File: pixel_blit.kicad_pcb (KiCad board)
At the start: 4 copper layers, 197.5 x 122 mm, 224 parts, among them CN1 PJ-3059-B, J1 DBT50G-9.5-2P, J10 DB301V-3.5-3P-GN, J11 DB301V-3.5-3P-GN, J12 DB301V-3.5-3P-GN, J13 DB301V-3.5-3P-GN, J14 DB301V-3.5-3P-GN, J15 DB301V-3.5-3P-GN, J16 DB301V-3.5-3P-GN, J17 DB301V-3.5-3P-GN, J18 DB301V-3.5-3P-GN, J19 DB301V-3.5-3P-GN, J2 DBT50G-9.5-2P, J20 DB301V-3.5-3P-GN, J21 DB301V-3.5-3P-GN, J22 DB301V-3.5-3P-GN, J23 DB301V-3.5-3P-GN, J24 DB301V-3.5-3P-GN, J25 DB301V-3.5-3P-GN, J26 DB301V-3.5-3P-GN, J27 DB301V-3.5-3P-GN, J28 DB301V-3.5-3P-GN, J29 DB301V-3.5-3P-GN, J3 DBT50G-9.5-2P, J30 DB301V-3.5-3P-GN, J31 DB301V-3.5-3P-GN, J32 DB301V-3.5-3P-GN, J33 DB301V-3.5-3P-GN, J34 DB301V-3.5-3P-GN, J35 DB301V-3.5-3P-GN, J36 DB301V-3.5-3P-GN, J37 Conn_01x03_Pin, J38 2.54-1*4, J4 DBT50G-9.5-2P, J5 DB301V-3.5-3P-GN, J6 DB301V-3.5-3P-GN, J7 DB301V-3.5-3P-GN, J8 DB301V-3.5-3P-GN, J9 DB301V-3.5-3P-GN, SW1 K2-1808SN-A4SW, SW2 SS-22D03-G040, U1 RP2350B_C42415655, U10 APS6404L-3SQR-SN, U2 W25Q128JVSIQTR, U3 TPS552872, U4 TPS62A02A, U5 SN74LVC8T245PWR, U6 SN74LVC8T245PWR, U7 SN74LVC8T245PWR, U8 SN74LVC8T245PWR, U9 RMC20452T

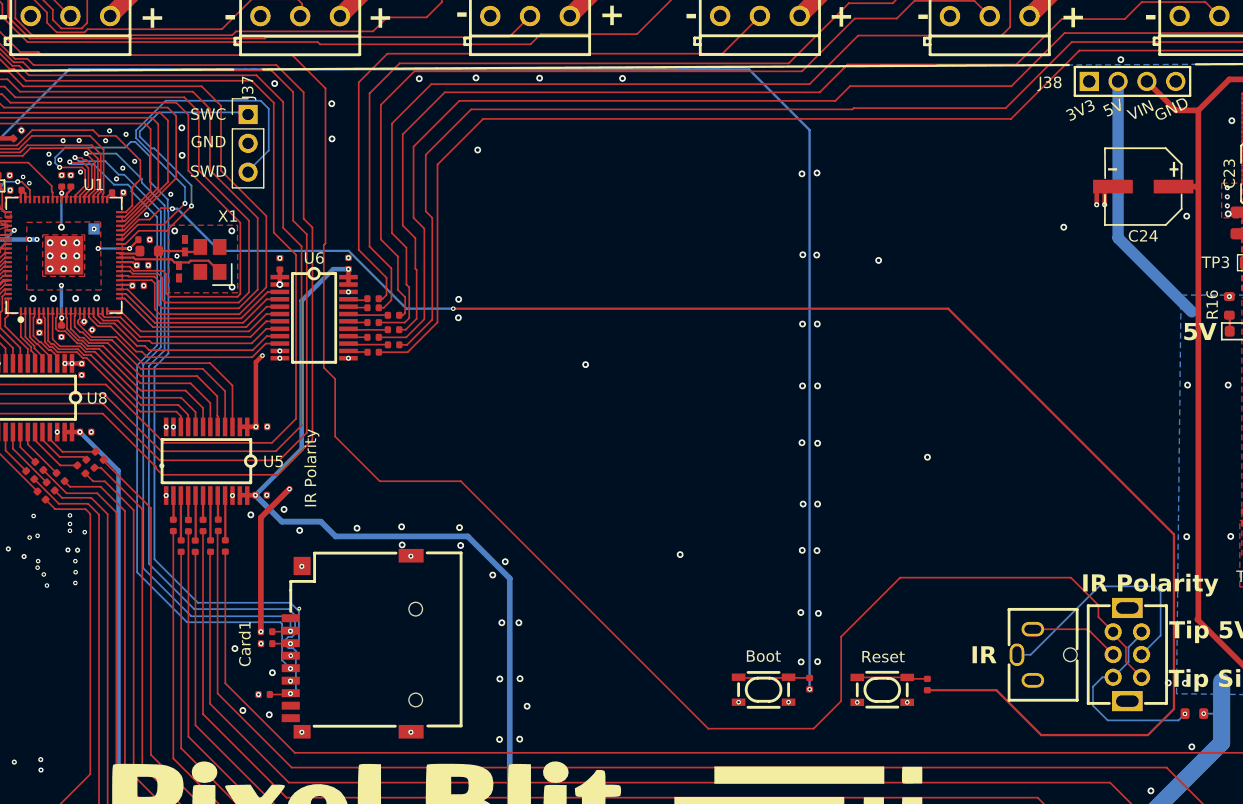
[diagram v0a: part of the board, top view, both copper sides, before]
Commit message: Move Boot/Reset beside the MCU, remove the QSPI_SS ground split
SW1/R1 and Reset1/R18 move into the old display area. QSPI_SS drops a
short B.Cu stub to R1 and RUN ends at R18, so the long QSPI_SS leg down
x=145.6 that split the back GND plane, its stitching vias, and the RUN
loop to x=178 are removed.
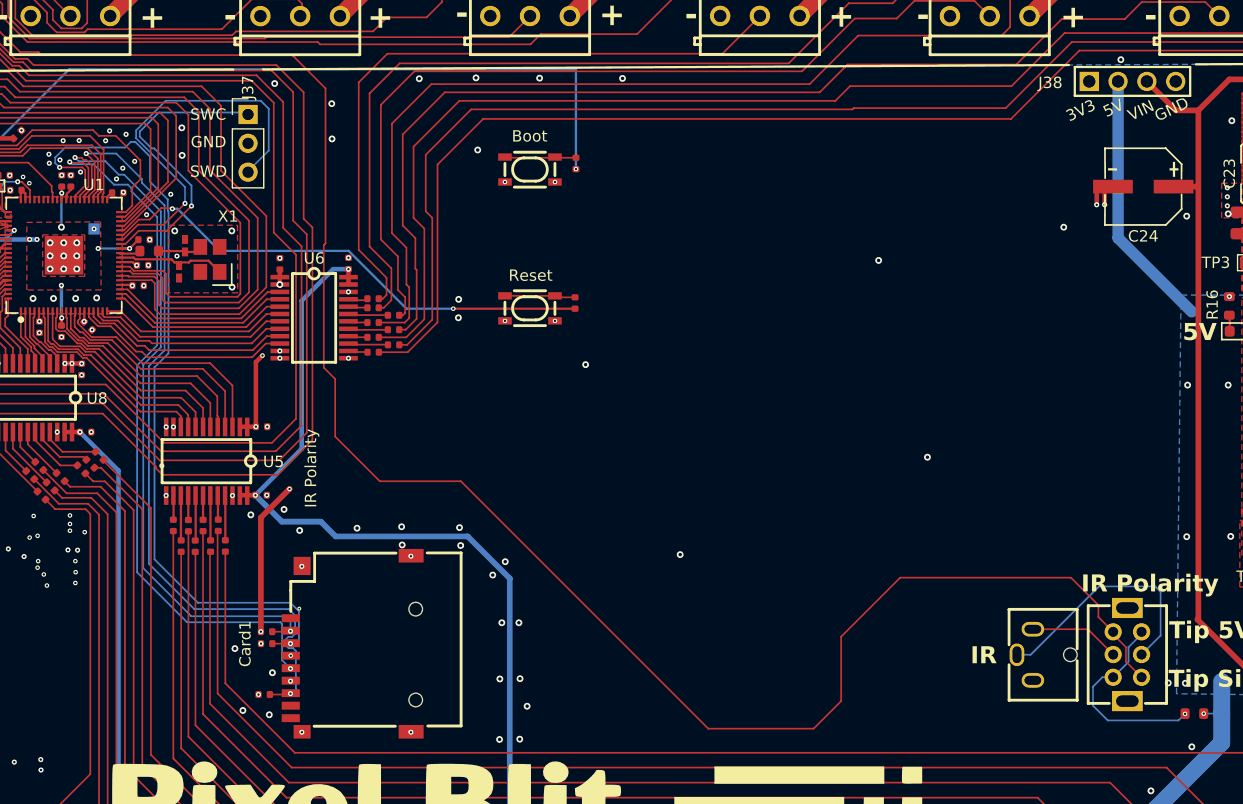
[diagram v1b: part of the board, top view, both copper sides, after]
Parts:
- moved R1 50.2 mm to (125.1, 64.5)
- moved SW1 50.2 mm to (121.0, 65.0)
- moved R18 45.7 mm to (125.0, 76.8)
- moved Reset1 45.7 mm to (121.0, 77.2)
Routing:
- net Net-(U1-RUN): track 145.4 -> 44.7 mm
- net Net-(U1-QSPI_SS): track 167.8 -> 104.5 mm
- net GND: vias 300 -> 282

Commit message: Add status RGB LED, user button and blown-fuse LEDs
- D14 common-cathode RGB (C601684) with R72-R74 on GPIO 41/44/45, SW3
  'Play' on GPIO 43; routed from U1 via short F.Cu escapes and In2 lanes
  to the old display area. GPIO 40 and 46 stay spare.
- D15-D18 red LEDs with 10k 0603 across each zone fuse, between holder
  and input terminal.
- Zone borders regenerated; plan doc GPIO map updated.
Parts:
- added D14: RGB, JLCImport:TJ-S1615CY6TGLCCSRGB-A5, F.Cu at (132.0, 71.0)
- added D15: Red, PixelBlit:D_0603, F.Cu at (226.4, 126.5)
- added D16: Red, PixelBlit:D_0603, F.Cu at (226.4, 100.3)
- added D17: Red, PixelBlit:D_0603, F.Cu at (226.4, 83.0)
- added D18: Red, PixelBlit:D_0603, F.Cu at (226.4, 56.0)
- added R68: 10kΩ, PixelBlit:R_0603, F.Cu at (226.4, 129.4)
- added R69: 10kΩ, PixelBlit:R_0603, F.Cu at (226.4, 103.2)
- added R70: 10kΩ, PixelBlit:R_0603, F.Cu at (226.4, 80.1)
- added R71: 10kΩ, PixelBlit:R_0603, F.Cu at (226.4, 53.1)
- added R72: 1kΩ, PixelBlit:R_0402, F.Cu at (128.6, 70.5)
- added R73: 1kΩ, PixelBlit:R_0402, F.Cu at (135.2, 70.5)
- added R74: 470Ω, PixelBlit:R_0402, F.Cu at (135.2, 71.8)
- added SW3: ~, PixelBlit:KEY-SMD_4P-L4.2-W3.2-P2.20-LS5.1-TL, F.Cu at (121.0, 89.0)
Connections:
- U1 pad 52: unconnected-(U1-GPIO41_ADC1-Pad52) -> /LED_R
- U1 pad 54: unconnected-(U1-GPIO43_ADC3-Pad54) -> /BTN_USER
- U1 pad 55: unconnected-(U1-GPIO44_ADC4-Pad55) -> /LED_G
- U1 pad 56: unconnected-(U1-GPIO45_ADC5-Pad56) -> /LED_B
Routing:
- net /LED_B: track 0.00 -> 66.9 mm, vias 0 -> 2
- net /BTN_USER: track 0.00 -> 65.9 mm, vias 0 -> 2
- net /LED_G: track 0.00 -> 65.6 mm, vias 0 -> 2
- net /LED_R: track 0.00 -> 55.5 mm, vias 0 -> 2
- net +12V_Z3: track 3.80 -> 6.48 mm, vias 43 -> 44
- net +12V_Z1: track 3.80 -> 6.18 mm, vias 43 -> 44
- net +12V_Z4: track 3.80 -> 6.08 mm, vias 43 -> 44
- net +12V_Z2: track 3.80 -> 5.98 mm, vias 43 -> 44
- net Net-(D14-R): track 0.00 -> 1.95 mm
- net Net-(D14-B): track 0.00 -> 1.87 mm
- net Net-(D14-G): track 0.00 -> 1.75 mm
- net Net-(D17-Pad1): track 0.00 -> 1.29 mm
- net Net-(D15-Pad1): track 0.00 -> 1.29 mm
- net Net-(D18-Pad1): track 0.00 -> 1.29 mm
- net Net-(D16-Pad1): track 0.00 -> 1.29 mm
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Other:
- board text added: "Play"
- board text added: "Status"

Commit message: Route status LED and button on the old display-panel lines
Replace the In2 lanes with the old TRB/TRA/PSH routes (red GPIO 43,
green GPIO 45, blue GPIO 41) and restore BAK (GPIO 40) for the Play
button. PSH's B.Cu tail moves to F.Cu beside TRB with a short hop under
IR_IN; Boot moves right to clear TRA; RUN via shifted 1 mm.
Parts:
- moved SW3 29.5 mm to (134.0, 62.5)
- moved R1 20.0 mm to (145.1, 65.5)
- moved SW1 20.0 mm to (141.0, 66.0)
- moved R73 11.2 mm to (125.5, 65.0), turned to 180 degrees
- moved R74 10.4 mm to (125.5, 68.0), turned to 180 degrees
- moved R72 5.30 mm to (125.5, 66.2)
- moved D14 5.06 mm to (129.5, 66.6)
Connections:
- U1 pad 49: unconnected-(U1-GPIO40_ADC0-Pad49) -> /BTN_USER
- U1 pad 52: /LED_R -> /LED_B
- U1 pad 54: /BTN_USER -> /LED_R
- U1 pad 55: /LED_G -> unconnected-(U1-GPIO44_ADC4-Pad55)
- U1 pad 56: /LED_B -> /LED_G
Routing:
- net /LED_R: track 55.5 -> 118.4 mm, vias 2 -> 0
- net /LED_G: track 65.6 -> 122.2 mm, vias 2 -> 0
- net /LED_B: track 66.9 -> 114.9 mm
- net Net-(U1-QSPI_SS): track 104.5 -> 125.5 mm
- net /BTN_USER: track 65.9 -> 71.7 mm, vias 2 -> 6
- net Net-(D14-G): track 1.75 -> 5.59 mm
- net Net-(D14-B): track 1.87 -> 5.40 mm
- net Net-(D14-R): track 1.95 -> 2.59 mm
